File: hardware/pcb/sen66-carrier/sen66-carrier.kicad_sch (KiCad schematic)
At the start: 10 parts, among them J1 SEN66 CABLE PADS, J2 TO MAIN J3

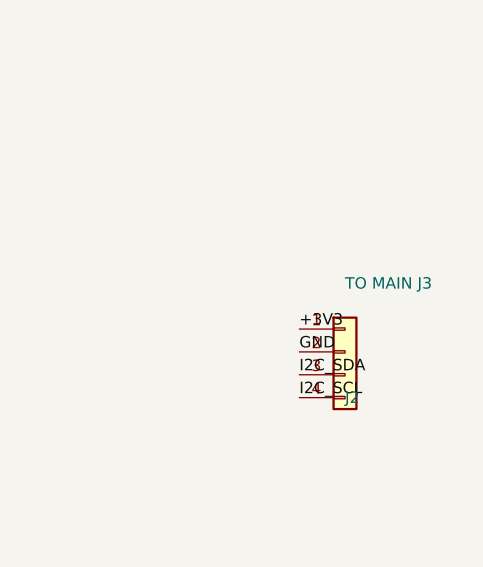
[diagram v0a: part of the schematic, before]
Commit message: Integrate JST PH connectors into schematics
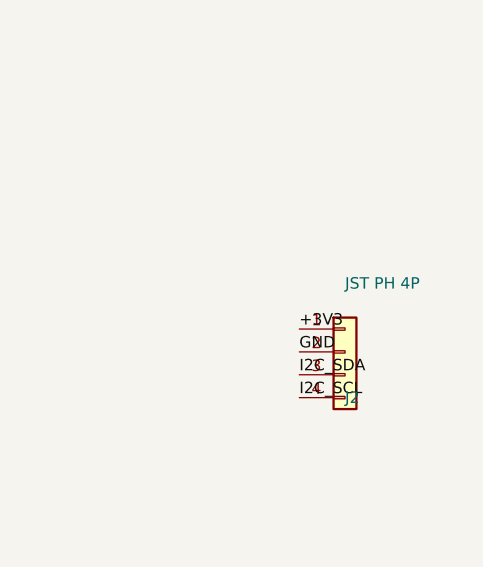
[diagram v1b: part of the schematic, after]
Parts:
- J2: value TO MAIN J3 -> JST PH 4P; footprint Connector_PinSocket_2.54mm:PinSocket_1x04_P2.54mm_Horizontal -> Connector_JST:JST_PH_S4B-PH-K_1x04_P2.00mm_Horizontal; Assembly (none) -> TH / hand solder or wave solder candidate; LCSC (none) -> C157926; Manufacturer (none) -> JST; Manufacturer Part Number 2.54 mm 1x04 RA socket -> S4B-PH-K-S(LF)(SN); Notes (none) -> Side-entry, keyed; main J3 matching; Status Hand solder; pin order matches main J3 -> Selected; manufacturing release blocked
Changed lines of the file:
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@@
 			)
 		)
-		(property "Value" "TO MAIN J3"
+		(property "Value" "JST PH 4P"
 			(at 204.47 82.55 0.0000)
 			(effects
@@
 			)
 		)
-		(property "Footprint" "Connector_PinSocket_2.54mm:PinSocket_1x04_P2.54mm_Horizontal"
+		(property "Footprint" "Connector_JST:JST_PH_S4B-PH-K_1x04_P2.00mm_Horizontal"
 			(at 204.47 90.17 0.0000)
 			(effects
@@
 			)
 		)
-		(property "Manufacturer Part Number" "2.54 mm 1x04 RA socket"
+		(property "Manufacturer Part Number" "S4B-PH-K-S(LF)(SN)"
 			(at 207.01 95.2499 0)
 			(effects
@@
 			)
 		)
-		(property "Status" "Hand solder; pin order matches main J3"
+		(property "Manufacturer" "JST"
 			(at 207.01 95.2499 0)
 			(effects
+				(font
+					(size 1.27 1.27)
+				)
+				(hide yes)
+			)
+		)
+		(property "LCSC" "C157926"
+			(at 207.01 95.2499 0)
+			(effects
+				(font
+					(size 1.27 1.27)
+				)
+				(hide yes)
+			)
+		)
+		(property "Assembly" "TH / hand solder or wave solder candidate"
+			(at 207.01 95.2499 0)
+			(effects
+				(font
+					(size 1.27 1.27)
+				)
+				(hide yes)
+			)
+		)
+		(property "Status" "Selected; manufacturing release blocked"
+			(at 207.01 95.2499 0)
+			(effects
+				(font
+					(size 1.27 1.27)
+				)
+				(hide yes)
+			)
+		)
+		(property "Notes" "Side-entry, keyed; main J3 matching"
+			(at 207.01 95.2499 0)
+			(effects
